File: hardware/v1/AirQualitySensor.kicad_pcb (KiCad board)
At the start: 2 copper layers, 4 parts, among them U1 004-0-0053, U2 DHT22

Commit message: More Layout work
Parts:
- added C1: 1u, Capacitor_SMD:C_0603_1608Metric, F.Cu at (124.0, 112.4)
- added C10: 1u, Capacitor_SMD:C_0402_1005Metric, F.Cu at (121.3, 86.4)
- added C11: 1u, Capacitor_SMD:C_0402_1005Metric, F.Cu at (118.1, 86.4)
- added C12: 1u, Capacitor_SMD:C_0402_1005Metric, F.Cu at (145.4, 86.4)
- added C13: 1u, Capacitor_SMD:C_0402_1005Metric, F.Cu at (114.9, 86.4)
- added C2: 1u, Capacitor_SMD:C_0603_1608Metric, F.Cu at (126.4, 110.0)
- added C3: 4u7, Capacitor_SMD:C_0603_1608Metric, F.Cu at (128.9, 116.1)
- added C4: 4u7, Capacitor_SMD:C_0603_1608Metric, F.Cu at (128.3, 110.0)
- added C5: 100u, Capacitor_SMD:C_0402_1005Metric, F.Cu at (128.9, 104.8)
- added C6: 1u, Capacitor_SMD:C_0402_1005Metric, F.Cu at (127.6, 86.4)
- added C7: 1u, Capacitor_SMD:C_0402_1005Metric, F.Cu at (133.2, 86.4)
- added C8: 1u, Capacitor_SMD:C_0402_1005Metric, F.Cu at (124.5, 86.4)
- added C9: 1u, Capacitor_SMD:C_0402_1005Metric, F.Cu at (137.0, 86.4)
- added FB1: 100R, Inductor_SMD:L_0603_1608Metric, F.Cu at (121.9, 116.8)
- added FB2: 100R, Inductor_SMD:L_0603_1608Metric, F.Cu at (120.5, 112.4)
- added J1: USB_C_Receptacle_USB2.0, Connector_USB:USB_C_Receptacle_HRO_TYPE-C-31-M-12, F.Cu at (108.6, 112.4)
- added R1: 5.1k, Resistor_SMD:R_0402_1005Metric, F.Cu at (110.5, 106.7)
- added R2: 5.1k, Resistor_SMD:R_0402_1005Metric, F.Cu at (110.5, 118.1)
- added R3: 10k, Resistor_SMD:R_0402_1005Metric, F.Cu at (174.6, 91.4)
- added R4: 10k, Resistor_SMD:R_0402_1005Metric, F.Cu at (177.2, 91.4)
- added R5: 10k, Resistor_SMD:R_0402_1005Metric, F.Cu at (132.2, 116.2)
- added U3: XC6206P332MR, Package_TO_SOT_SMD:SOT-23, F.Cu at (123.8, 109.9)
- moved A1 4.68 mm to (119.4, 97.8)
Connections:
- net Net-(DS1-Pad36) renamed DISP_SI
- net Net-(DS1-Pad37) renamed DISP_SCL
- net Net-(DS1-Pad38) renamed DISP_A0
- net Net-(DS1-Pad39) renamed DISP_RST
- net Net-(DS1-Pad40) renamed DISP_CS
- A1 pad 22: +5V -> VBUS
- A1 pad 23: Net-(A1-Pad23) -> USB_D-
- A1 pad 24: Net-(A1-Pad24) -> USB_D+
- DS1 pad 26: Net-(DS1-Pad26) -> GND
- DS1 pad 31: Net-(DS1-Pad31) -> Net-(C12-Pad1)
- DS1 pad 32: Net-(DS1-Pad32) -> Net-(C12-Pad1)
- DS1 pad 33: Net-(DS1-Pad33) -> GND
- DS1 pad 34: Net-(DS1-Pad34) -> +3V3
- DS1 pad 35: Net-(DS1-Pad35) -> +3V3
- U1 pad 1: Net-(U1-Pad1) -> +5V
- U1 pad 2: Net-(U1-Pad2) -> GND
- U1 pad 7: Net-(U1-Pad7) -> S8_RXD
- U1 pad 8: Net-(U1-Pad8) -> S8_TXD
- U2 pad 1: Net-(U2-Pad1) -> +5V
- U2 pad 2: Net-(U2-Pad2) -> DHT22
- U2 pad 4: Net-(U2-Pad4) -> GND

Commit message: Continue schematic
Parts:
- added C14: 100u, Capacitor_SMD:C_0402_1005Metric, F.Cu at (148.6, 86.4)
- added J2: SWD, AirQualitySensor:TC2030-IDC-FP, F.Cu at (102.9, 96.5)
- added J3: UART, Connector_PinHeader_2.54mm:PinHeader_1x06_P2.54mm_Vertical, F.Cu at (142.2, 120.7)
- moved DS1 2.90 mm to (167.6, 115.6)
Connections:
- A1 pad 21: Net-(A1-Pad21) -> RESET
- A1 pad 27: Net-(A1-Pad27) -> SWD_SWO
- A1 pad 31: Net-(A1-Pad31) -> SWD_SWCLK
- A1 pad 32: Net-(A1-Pad32) -> SWD_SWDIO
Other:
- board outline added: 81.3 x 36.8 mm

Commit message: More layouting
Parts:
- added D1: Red, LED_THT:LED_D3.0mm, B.Cu at (177.8, 110.5)
- added D2: Yellow, LED_THT:LED_D3.0mm, B.Cu at (177.8, 104.6)
- added D3: Green, LED_THT:LED_D3.0mm, B.Cu at (177.8, 98.7)
- added H1: MountingHole, MountingHole:MountingHole_2.5mm_Pad, F.Cu at (110.5, 106.7)
- added H2: MountingHole, MountingHole:MountingHole_2.5mm_Pad, F.Cu at (175.3, 88.9)
- added H3: MountingHole, MountingHole:MountingHole_2.5mm_Pad, F.Cu at (184.2, 115.6)
- added R6: 10k, Resistor_SMD:R_0402_1005Metric, F.Cu at (147.3, 99.8)
- added R7: 10k, Resistor_SMD:R_0402_1005Metric, F.Cu at (145.8, 99.8)
- added R8: 100k, Resistor_SMD:R_0402_1005Metric, F.Cu at (144.3, 99.8)
- moved J2 77.5 mm to (177.5, 117.2), turned to 90 degrees
- moved A1 28.6 mm to (144.3, 112.0), turned to 180 degrees
- moved J3 27.4 mm to (169.7, 119.9)
- moved C4 23.0 mm to (111.0, 94.7), turned to 0 degrees
- moved C5 21.6 mm to (150.4, 102.4), turned to 180 degrees
- moved C2 20.3 mm to (111.0, 96.6), turned to 0 degrees
- moved R5 18.9 mm to (141.2, 99.6), turned to 180 degrees
- moved C1 17.0 mm to (113.4, 99.0), turned to 270 degrees
- moved U3 16.8 mm to (110.9, 99.2), turned to 270 degrees
- moved R3 16.6 mm to (186.7, 102.9), turned to 180 degrees
- moved C6 13.3 mm to (117.1, 94.5), turned to 180 degrees
- moved R4 13.0 mm to (186.7, 100.3), turned to 180 degrees
- moved FB2 12.2 mm to (113.4, 102.5), turned to 270 degrees
- moved U2 10.4 mm to (128.0, 114.3)
- moved C8 10.1 mm to (117.1, 93.2), turned to 180 degrees
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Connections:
- C10 pad 1: GND -> Net-(C10-Pad1)
- C10 pad 2: Net-(C10-Pad2) -> GND
- C11 pad 1: GND -> Net-(C11-Pad1)
- C11 pad 2: Net-(C11-Pad2) -> GND
- C12 pad 1: Net-(C12-Pad1) -> GND
- C12 pad 2: GND -> Net-(C12-Pad2)
- C13 pad 1: GND -> Net-(C13-Pad1)
- C13 pad 2: Net-(C13-Pad2) -> GND
- C14 pad 1: GND -> +3V3
- C14 pad 2: +3V3 -> GND
- C5 pad 1: +3V3 -> GND
- C5 pad 2: GND -> +3V3
- C6 pad 1: GND -> Net-(C6-Pad1)
- C6 pad 2: Net-(C6-Pad2) -> GND
- C8 pad 1: GND -> Net-(C8-Pad1)
- C8 pad 2: Net-(C8-Pad2) -> GND
- DS1 pad 21: Net-(C13-Pad2) -> Net-(C13-Pad1)
- DS1 pad 22: Net-(C11-Pad2) -> Net-(C11-Pad1)
- DS1 pad 23: Net-(C10-Pad2) -> Net-(C10-Pad1)
- DS1 pad 24: Net-(C8-Pad2) -> Net-(C8-Pad1)
- DS1 pad 25: Net-(C6-Pad2) -> Net-(C6-Pad1)
- DS1 pad 27: Net-(C7-Pad1) -> Net-(C7-Pad2)
- DS1 pad 28: Net-(C7-Pad2) -> Net-(C7-Pad1)
- DS1 pad 29: Net-(C9-Pad1) -> Net-(C9-Pad2)
- DS1 pad 30: Net-(C9-Pad2) -> Net-(C9-Pad1)
- DS1 pad 31: Net-(C12-Pad1) -> Net-(C12-Pad2)
- DS1 pad 32: Net-(C12-Pad1) -> Net-(C12-Pad2)
- R2 pad 1: GND -> Net-(J1-PadB5)
- R2 pad 2: Net-(J1-PadB5) -> GND
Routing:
- net VBUS: track 0.00 -> 92.2 mm, vias 0 -> 9
- net +3V3: track 0.00 -> 77.7 mm
- net GND: track 0.00 -> 69.7 mm, vias 0 -> 14
- net Net-(D1-Pad2): track 0.00 -> 43.2 mm
- net Net-(D2-Pad2): track 0.00 -> 39.0 mm
- net Net-(D3-Pad2): track 0.00 -> 36.6 mm
- net Net-(C6-Pad1): track 0.00 -> 15.7 mm
- net Net-(C8-Pad1): track 0.00 -> 12.2 mm
- net Net-(C10-Pad1): track 0.00 -> 8.81 mm
- net Net-(J1-PadA5): track 0.00 -> 6.22 mm
- net Net-(J1-PadB5): track 0.00 -> 6.16 mm
- net Net-(C11-Pad1): track 0.00 -> 5.61 mm
- net +5V: track 0.00 -> 5.31 mm
- net Net-(C1-Pad2): track 0.00 -> 4.38 mm
- net Net-(C12-Pad2): track 0.00 -> 4.08 mm
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- added copper zone on B.Cu, net GND
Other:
- outline, holes or cut-outs redrawn
- board text added: "5V"
- board text added: "GND"
- board text added: "RXD"
- board text added: "SWD"
- board text added: "TXD"
- board text added: "UART"

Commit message: More layouting
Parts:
- added R10: 10k, Resistor_SMD:R_0402_1005Metric, F.Cu at (157.0, 115.3)
- added R9: 10k, Resistor_SMD:R_0402_1005Metric, F.Cu at (160.0, 115.3)
- moved R5 17.7 mm to (134.1, 115.8), turned to 90 degrees
- moved R6 3.30 mm to (150.4, 98.6)
- moved R7 3.30 mm to (148.8, 98.6)
- moved R8 3.30 mm to (147.3, 98.6)
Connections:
- A1 pad 10: Net-(A1-Pad10) -> LED_GREEN
- A1 pad 11: Net-(A1-Pad11) -> LED_YELLOW
- A1 pad 12: Net-(A1-Pad12) -> LED_RED
- A1 pad 16: Net-(A1-Pad16) -> DISP_CS
- A1 pad 17: Net-(A1-Pad17) -> DISP_RST
- A1 pad 18: Net-(A1-Pad18) -> DISP_A0
- A1 pad 19: Net-(A1-Pad19) -> DISP_SCL
- A1 pad 2: Net-(A1-Pad2) -> UART_TXD
- A1 pad 20: Net-(A1-Pad20) -> DISP_SI
- A1 pad 3: Net-(A1-Pad3) -> UART_RXD
- A1 pad 34: Net-(A1-Pad34) -> DHT22
- A1 pad 8: Net-(A1-Pad8) -> S8_RXD
- A1 pad 9: Net-(A1-Pad9) -> S8_TXD
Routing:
- net +3V3: track 77.7 -> 188.5 mm, vias 0 -> 4
- net +5V: track 5.31 -> 56.2 mm, vias 0 -> 1
- net USB_D+: track 0.00 -> 41.6 mm
- net S8_TXD: track 0.00 -> 40.9 mm, vias 0 -> 4
- net S8_RXD: track 0.00 -> 39.3 mm, vias 0 -> 2
- net USB_D-: track 3.17 -> 37.2 mm
- net DISP_CS: track 0.00 -> 32.6 mm
- net DISP_RST: track 0.00 -> 30.3 mm
- net DISP_A0: track 0.00 -> 28.1 mm
- net DISP_SCL: track 0.00 -> 26.2 mm
- net DISP_SI: track 0.00 -> 24.4 mm
- net Net-(J1-PadS1): track 0.00 -> 17.0 mm
- net UART_RXD: track 0.00 -> 15.8 mm
- net UART_TXD: track 0.00 -> 12.2 mm
- net LED_GREEN: track 0.00 -> 12.1 mm, vias 0 -> 2
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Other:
- net class USB Data added: clearance 0.1524, trace_width 0.2, via_dia 0.8, via_drill 0.4

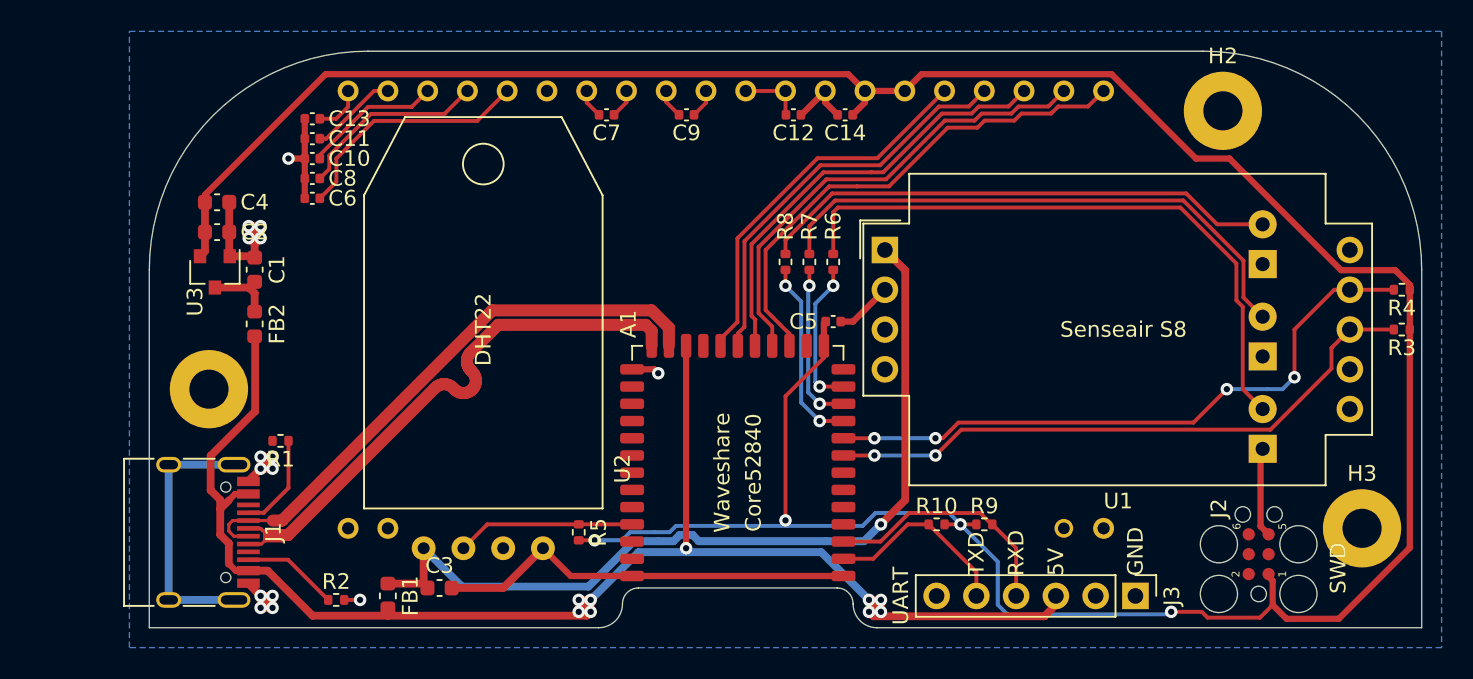
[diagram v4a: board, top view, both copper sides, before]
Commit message: Finish first layout
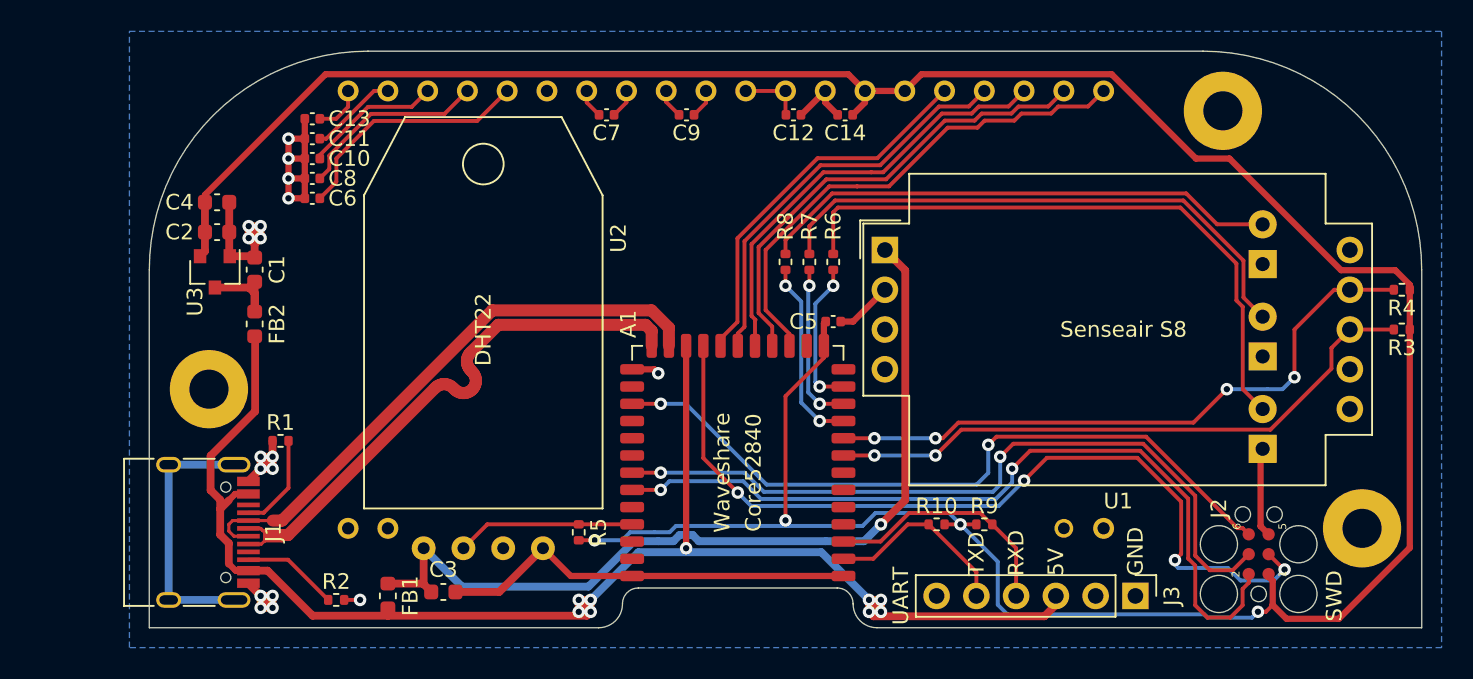
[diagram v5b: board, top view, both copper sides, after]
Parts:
- moved C3 0.35 mm to (125.5, 119.6)
- turned C2 to 180 degrees
- turned C4 to 180 degrees
- turned R1 to 0 degrees
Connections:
- C2 pad 1: +3V3 -> GND
- C2 pad 2: GND -> +3V3
- C4 pad 1: +3V3 -> GND
- C4 pad 2: GND -> +3V3
- R1 pad 1: Net-(J1-PadA5) -> GND
- R1 pad 2: GND -> Net-(J1-PadA5)
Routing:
- net RESET: track 0.00 -> 54.7 mm, vias 0 -> 4
- net SWD_SWDIO: track 0.00 -> 52.1 mm, vias 0 -> 2
- net SWD_SWCLK: track 0.00 -> 48.3 mm, vias 0 -> 2
- net SWD_SWO: track 0.00 -> 46.4 mm, vias 0 -> 2
- net GND: track 70.7 -> 78.6 mm, vias 15 -> 18
- net Net-(C1-Pad2): track 4.38 -> 6.29 mm

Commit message: Move sensor pins to high drive output pins
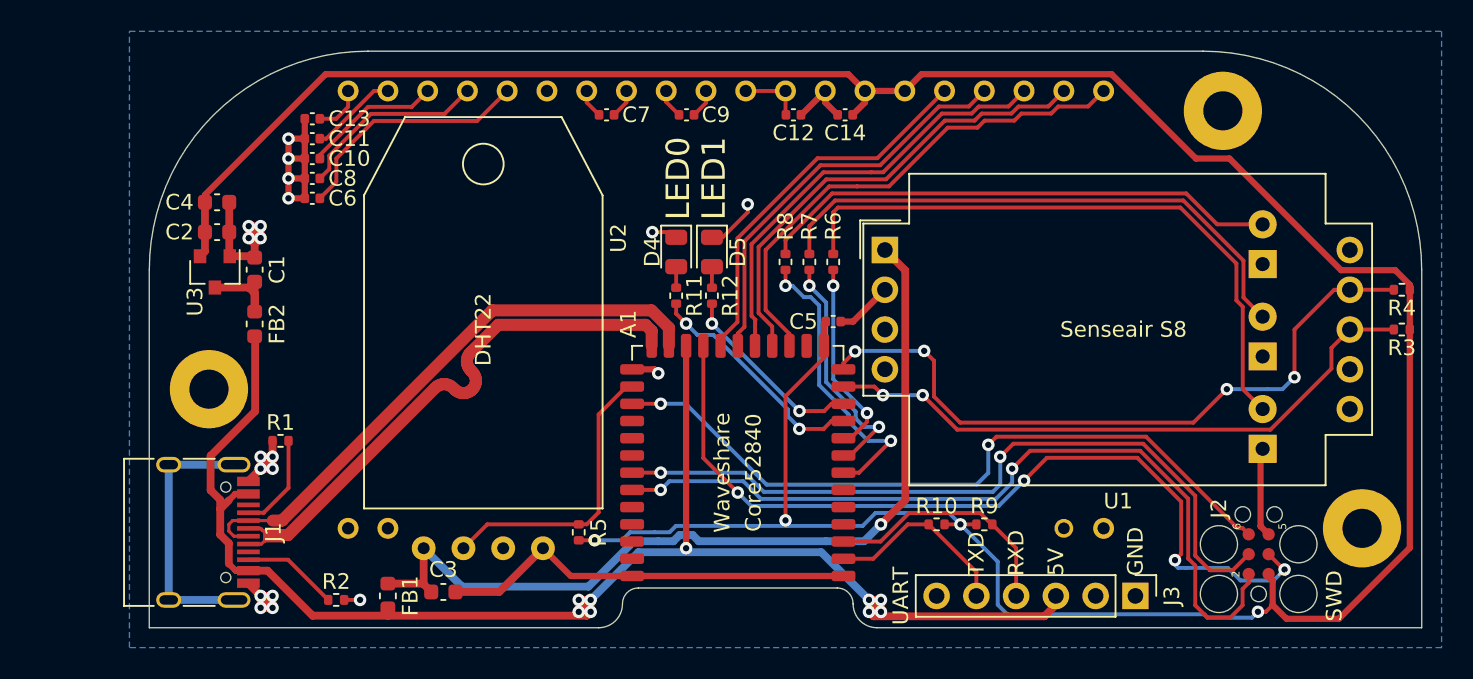
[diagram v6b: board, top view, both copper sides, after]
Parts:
- added D4: Status0, LED_SMD:LED_0805_2012Metric, F.Cu at (140.3, 97.9)
- added D5: Status0, LED_SMD:LED_0805_2012Metric, F.Cu at (142.6, 97.9)
- added R11: 20k, Resistor_SMD:R_0402_1005Metric, F.Cu at (140.3, 100.7)
- added R12: 20k, Resistor_SMD:R_0402_1005Metric, F.Cu at (142.6, 100.7)
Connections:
- A1 pad 10: LED_GREEN -> LED_STATUS0
- A1 pad 11: LED_YELLOW -> LED_STATUS1
- A1 pad 12: LED_RED -> S8_RXD
- A1 pad 13: Net-(A1-Pad13) -> S8_TXD
- A1 pad 26: Net-(A1-Pad26) -> DHT22
- A1 pad 34: DHT22 -> Net-(A1-Pad34)
- A1 pad 7: Net-(A1-Pad7) -> LED_GREEN
- A1 pad 8: S8_RXD -> LED_YELLOW
- A1 pad 9: S8_TXD -> LED_RED
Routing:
- net LED_STATUS0: track 0.00 -> 14.9 mm, vias 0 -> 2
- net LED_STATUS1: track 0.00 -> 12.2 mm, vias 0 -> 2
- net DHT22: track 11.4 -> 18.7 mm
- net LED_GREEN: track 12.1 -> 19.0 mm
- net GND: track 78.6 -> 84.2 mm, vias 18 -> 20
- net LED_YELLOW: track 10.4 -> 15.5 mm
- net S8_TXD: track 40.9 -> 44.4 mm
- net LED_RED: track 9.56 -> 12.5 mm
- net Net-(D5-Pad2): track 0.00 -> 1.34 mm
- net Net-(D4-Pad2): track 0.00 -> 1.34 mm
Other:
- board text added: "LED0"
- board text added: "LED1"

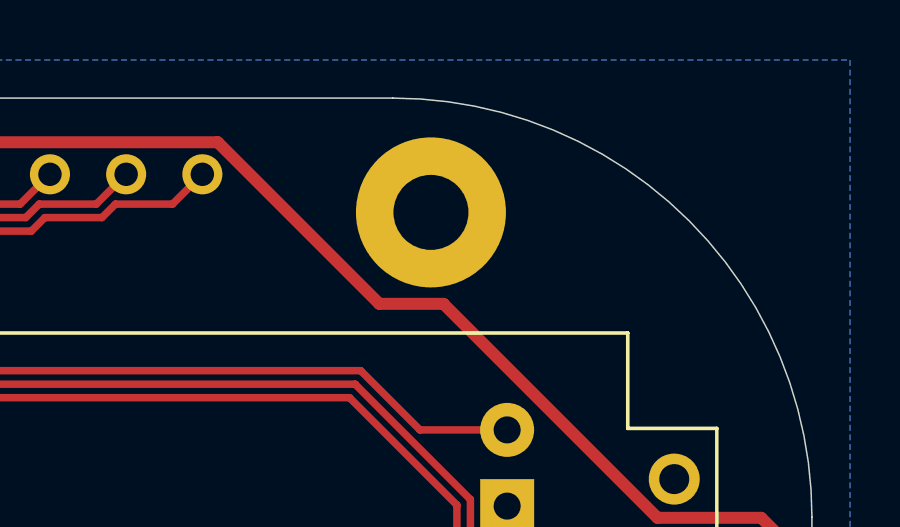
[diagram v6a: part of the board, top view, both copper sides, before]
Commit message: Increase clearing between display and screw hole
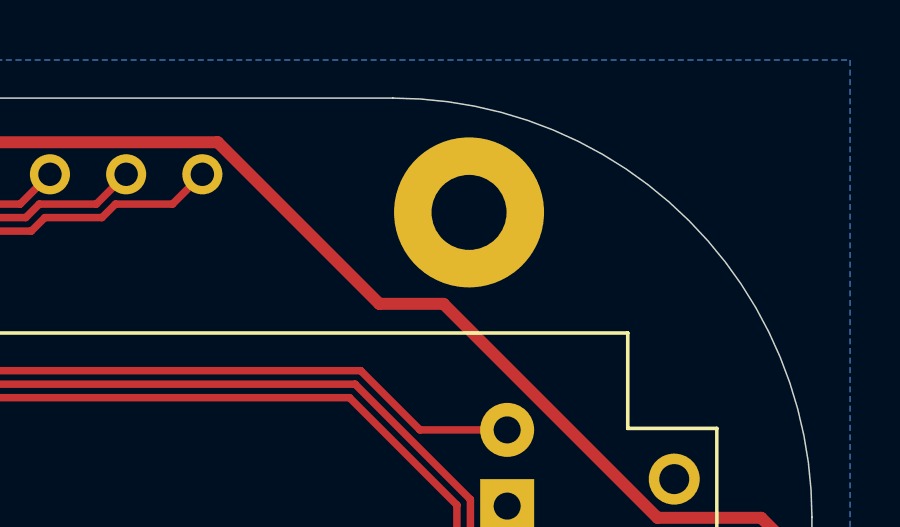
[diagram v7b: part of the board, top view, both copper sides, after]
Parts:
- moved H2 1.27 mm to (176.5, 88.9)
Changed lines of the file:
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@@
   )
   (module MountingHole:MountingHole_2.5mm_Pad (layer F.Cu)
-    (at 175.26 88.9)
+    (at 176.53 88.9)
     (descr "Mounting Hole 2.5mm")
     (tags "mounting hole 2.5mm")

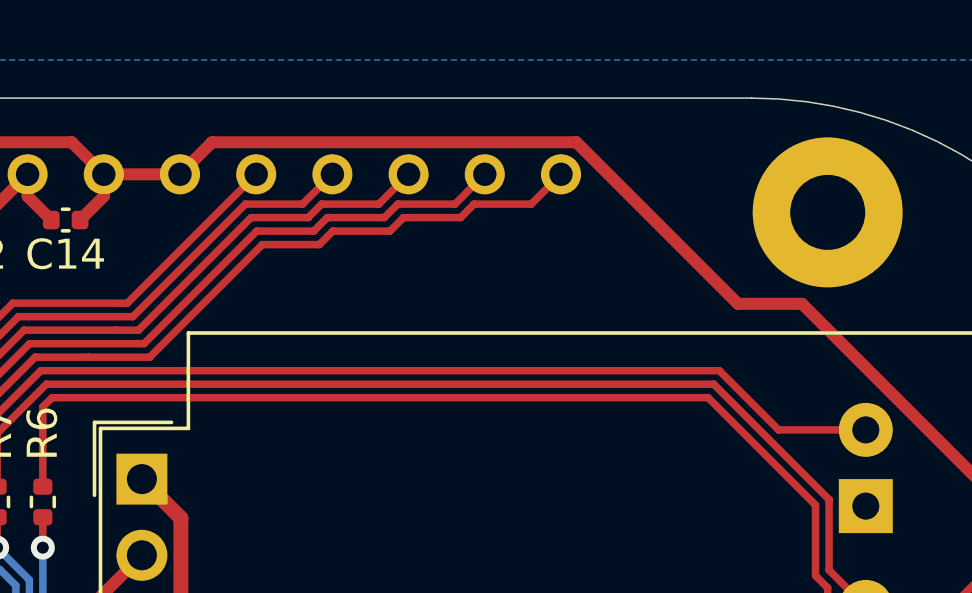
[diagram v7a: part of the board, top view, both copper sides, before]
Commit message: Add PCB Name and manufacturer ID
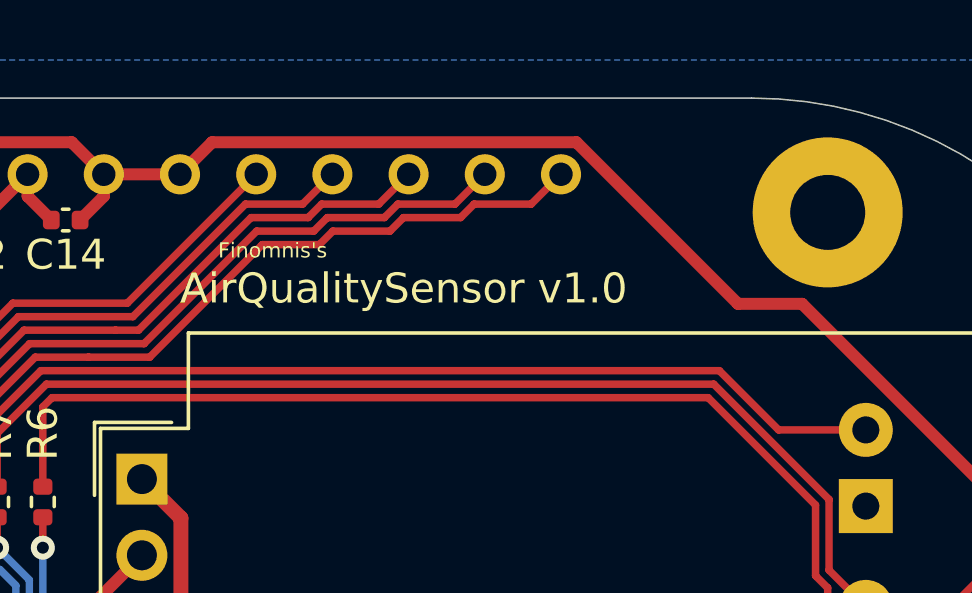
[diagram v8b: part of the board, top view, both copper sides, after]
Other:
- board text added: "AirQualitySensor v1.0"
- board text added: "Finomnis's"
- board text added: "JLCJLCJLCJLC"
- board text added: "PCB ID:"
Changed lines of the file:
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@@
   (general
     (thickness 1.6)
-    (drawings 20)
+    (drawings 24)
     (tracks 586)
     (zones 0)
@@
   (page A4)
   (layers
-    (0 F.Cu signal)
+    (0 F.Cu signal hide)
     (31 B.Cu signal)
-    (32 B.Adhes user)
-    (33 F.Adhes user)
+    (32 B.Adhes user hide)
+    (33 F.Adhes user hide)
     (34 B.Paste user)
-    (35 F.Paste user)
+    (35 F.Paste user hide)
     (36 B.SilkS user)
-    (37 F.SilkS user)
+    (37 F.SilkS user hide)
     (38 B.Mask user)
-    (39 F.Mask user)
-    (40 Dwgs.User user)
-    (41 Cmts.User user)
-    (42 Eco1.User user)
-    (43 Eco2.User user)
+    (39 F.Mask user hide)
+    (40 Dwgs.User user hide)
+    (41 Cmts.User user hide)
+    (42 Eco1.User user hide)
+    (43 Eco2.User user hide)
     (44 Edge.Cuts user)
-    (45 Margin user)
+    (45 Margin user hide)
     (46 B.CrtYd user)
-    (47 F.CrtYd user)
+    (47 F.CrtYd user hide)
     (48 B.Fab user)
-    (49 F.Fab user)
+    (49 F.Fab user hide)
   )
   (setup
@@
       (net 55 LED_GREEN))
   )
+  (gr_text "PCB ID:" (at 133.35 109.22) (layer B.SilkS)
+    (effects (font (size 1 1) (thickness 0.15)) (justify mirror))
+  )
+  (gr_text JLCJLCJLCJLC (at 124.46 109.22) (layer B.SilkS)
+    (effects (font (size 1 1) (thickness 0.15)) (justify mirror))
+  )
+  (gr_text Finomnis's (at 156.21 90.17) (layer F.SilkS)
+    (effects (font (size 0.5 0.5) (thickness 0.065)) (justify left))
+  )
+  (gr_text "AirQualitySensor v1.0" (at 154.94 91.44) (layer F.SilkS)
+    (effects (font (size 1 1) (thickness 0.15)) (justify left))
+  )
   (gr_text LED1 (at 142.748 93.218 90) (layer F.SilkS)
